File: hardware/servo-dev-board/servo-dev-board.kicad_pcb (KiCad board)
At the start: 2 copper layers, 50 x 30 mm, 39 parts, among them J1 Conn_01x04, J2 Conn_01x05, J3 Conn_01x04, J4 Conn_02x05_Odd_Even, SW1 SW_Push, SW2 SW_Push, U1 DRV8231ADSGR, U2 SSP7615-33DFR, U3 STM32F301K8Ux, Y1 16MHz 9pF

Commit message: design pcb
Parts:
- removed D1: SS34, Diode_SMD:D_SMA
- removed H3, H4, H5, H6: MountingHole, MountingHole:MountingHole_2.2mm_M2_DIN965_Pad
- added MH1: MountingHole_Pad_MP, MountingHole:MountingHole_2.2mm_M2_Pad_Via, F.Cu at (118.0, 93.0)
- added MH2: MountingHole_Pad_MP, MountingHole:MountingHole_2.2mm_M2_Pad_Via, F.Cu at (118.0, 109.0)
- added MH3: MountingHole_Pad_MP, MountingHole:MountingHole_2.2mm_M2_Pad_Via, F.Cu at (162.0, 109.0)
- added MH4: MountingHole_Pad_MP, MountingHole:MountingHole_2.2mm_M2_Pad_Via, F.Cu at (162.0, 93.0)
- J2: value Conn_01x05 -> Conn_01x05_MountingPin; footprint Connector_JST:JST_SH_SM05B-SRSS-TB_1x05-1MP_P1.00mm_Horizontal -> Connector_JST:JST_ZH_B5B-ZR-SM4-TF_1x05-1MP_P1.50mm_Vertical
- J3: value Conn_01x04 -> Conn_01x04_MountingPin
- J4: renamed from J1; value Conn_01x04 -> Conn_01x04_MountingPin
- moved R7 93.7 mm to (127.3, 97.8), turned to -90 degrees
- moved R6 93.0 mm to (122.3, 111.3), turned to 90 degrees
- moved C10 89.5 mm to (142.9, 101.8), turned to 90 degrees
- moved L1 85.1 mm to (141.9, 101.8), turned to -90 degrees
- moved C5 84.7 mm to (123.4, 101.1), turned to 90 degrees
- moved C9 83.8 mm to (143.9, 101.8), turned to 90 degrees
- moved R5 82.2 mm to (128.2, 106.7)
- moved C4 81.7 mm to (123.0, 97.4)
- moved C8 79.1 mm to (146.3, 95.7), turned to 180 degrees
- moved C2 76.2 mm to (122.3, 90.7), turned to 90 degrees
- moved C3 74.6 mm to (121.3, 111.3), turned to 90 degrees
- moved C6 70.0 mm to (145.7, 97.0), turned to 180 degrees
- moved C7 67.7 mm to (150.2, 104.4)
- moved C1 65.3 mm to (124.4, 101.1), turned to 90 degrees
- moved R4 49.5 mm to (155.9, 106.4), turned to 180 degrees
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- renumbered USB1 to J1, J4 to J5
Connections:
- net /OSC_IN renamed /OSC-
- net /OSC_OUT renamed /OSC+
- J1 pad 1: /VBUS -> +5V
- J2 pad 1: /M1 -> /POT
- J2 pad 2: /M2 -> /VREF
- J2 pad 3: /VREF -> GND
- J2 pad 4: GND -> /M1
- J2 pad 5: /POT -> /M2
- J2 pad MP: (no net) -> GND
- J3 pad MP: (no net) -> GND
- J4 pad 1: /UART1_TX -> /UART1_RX
- J4 pad 3: /UART1_RX -> /UART1_TX
- J4 pad MP: (no net) -> GND
- R1 pad 1: /UART1_TX -> /UART1_RX
- R4 pad 1: /UART1_RX -> /UART1_TX
- U1 pad 4: /VREF -> +3V3
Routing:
- net /BOOT0: track 0.00 -> 52.9 mm, vias 0 -> 2
- net GND: track 0.00 -> 44.9 mm, vias 0 -> 37
- net /PWM2: track 0.00 -> 44.4 mm, vias 0 -> 2
- net /PWM1: track 0.00 -> 40.9 mm, vias 0 -> 2
- net +3V3: track 0.00 -> 31.9 mm, vias 0 -> 13
- net /ISNS: track 0.00 -> 30.5 mm, vias 0 -> 2
- net /NRST: track 0.00 -> 29.1 mm
- net /VREF: track 0.00 -> 22.4 mm, vias 0 -> 2
- net /I2C1_SDA: track 0.00 -> 19.2 mm
- net /PA2: track 0.00 -> 18.1 mm
- net /JTCK_SWCLK: track 0.00 -> 17.6 mm
- net /JTDO_SWO: track 0.00 -> 17.5 mm
- net /NJTRST: track 0.00 -> 16.4 mm
- net /PA3: track 0.00 -> 16.3 mm
- net /JTMS_SWDIO: track 0.00 -> 16.0 mm
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- added copper zone on In2.Cu, net +3V3
- added copper zone on F.Cu, net +5V
- added copper zone on In1.Cu, net GND
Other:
- board size 50 x 30 mm -> 51.5 x 23.5 mm
- copper layers 2 -> 4
- board text added: "."
- board text added: "3V3"
- board text added: "5V"
- board text added: "A12"
- board text added: "A2"
- board text added: "A3"
- board text added: "A4"
- board text added: "A5"
- board text added: "A6"
- board text added: "A7"
- board text added: "B0"
- board text added: "B5"
- board text added: "BOOT0"
- board text added: "G"
- board text added: "I2C"
- board text added: "JTAG/SWD"
- board text added: "MOTOR"
- board text added: "PWR"
- board text added: "RESET"
- board text added: "UART"
- board text added: "USB"
- board text added: "VREF"

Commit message: update servo-dev-board
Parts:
- added C11: 22uF, Capacitor_SMD:C_0603_1608Metric, F.Cu at (123.8, 98.8)
- J5: footprint Connector_PinSocket_1.27mm:PinSocket_2x05_P1.27mm_Vertical_SMD -> lib:IDC-TH_10P-P1.27-X1270WV-2X05A-6TV01
- R1, R2, R3, R4, R6: value 10K -> 4K7
- U1: footprint Package_SON:WSON-8-1EP_2x2mm_P0.5mm_EP0.9x1.6mm_ThermalVias -> Package_SON:WSON-8-1EP_2x2mm_P0.5mm_EP0.9x1.6mm
- moved C4 7.23 mm to (123.2, 104.6), turned to 180 degrees
- moved R7 5.27 mm to (131.1, 94.1), turned to 0 degrees
- moved U2 4.00 mm to (123.1, 103.1), turned to 90 degrees
- moved C5 2.30 mm to (124.4, 103.2)
- moved C1 1.78 mm to (125.0, 99.4)
- moved U1 1.66 mm to (125.8, 96.8)
- moved J3 1.55 mm to (154.9, 90.8)
- moved R2 1.55 mm to (157.8, 94.0)
- moved R3 1.55 mm to (155.9, 94.0)
- moved C2 1.52 mm to (122.3, 89.2)
- moved SW1 1.52 mm to (125.7, 90.1)
- moved J4 1.50 mm to (154.9, 111.1)
- moved MH1 1.50 mm to (118.0, 91.5)
- moved MH2 1.50 mm to (118.0, 110.5)
- moved MH3 1.50 mm to (162.0, 110.5)
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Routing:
- net GND: track 44.9 -> 16.4 mm, vias 37 -> 59
- net +3V3: track 31.9 -> 7.02 mm, vias 13 -> 16
- net +5V: track 15.8 -> 27.9 mm
- net /BOOT0: track 52.9 -> 40.8 mm
- net /M1: track 11.0 -> 0.00 mm
- net /M2: track 9.67 -> 0.00 mm
- net /PWM2: track 44.4 -> 36.7 mm
- net /NRST: track 29.1 -> 36.7 mm, vias 0 -> 2
- net /JTCK_SWCLK: track 17.6 -> 13.1 mm
- net /PWM1: track 40.9 -> 37.0 mm
- net /JTMS_SWDIO: track 16.0 -> 13.4 mm
- net /JTDO_SWO: track 17.5 -> 14.9 mm
- net /PA12: track 12.2 -> 14.0 mm
- net /NJTRST: track 16.4 -> 14.7 mm
- net /UART1_TX: track 11.1 -> 12.6 mm
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- added copper zone on F.Cu, net /M1
- added copper zone on F.Cu, net /M2
- added copper zone on B.Cu, net GND
- added copper zone on F.Cu, net GND
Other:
- board size 51.5 x 23.5 mm -> 51.5 x 26.5 mm
- board text added: "JLCJLCJLCJLC"
- board text added: "SERVO"
- board text added: "VRF"
- board text removed: "."
- board text removed: "MOTOR"
- board text removed: "VREF"

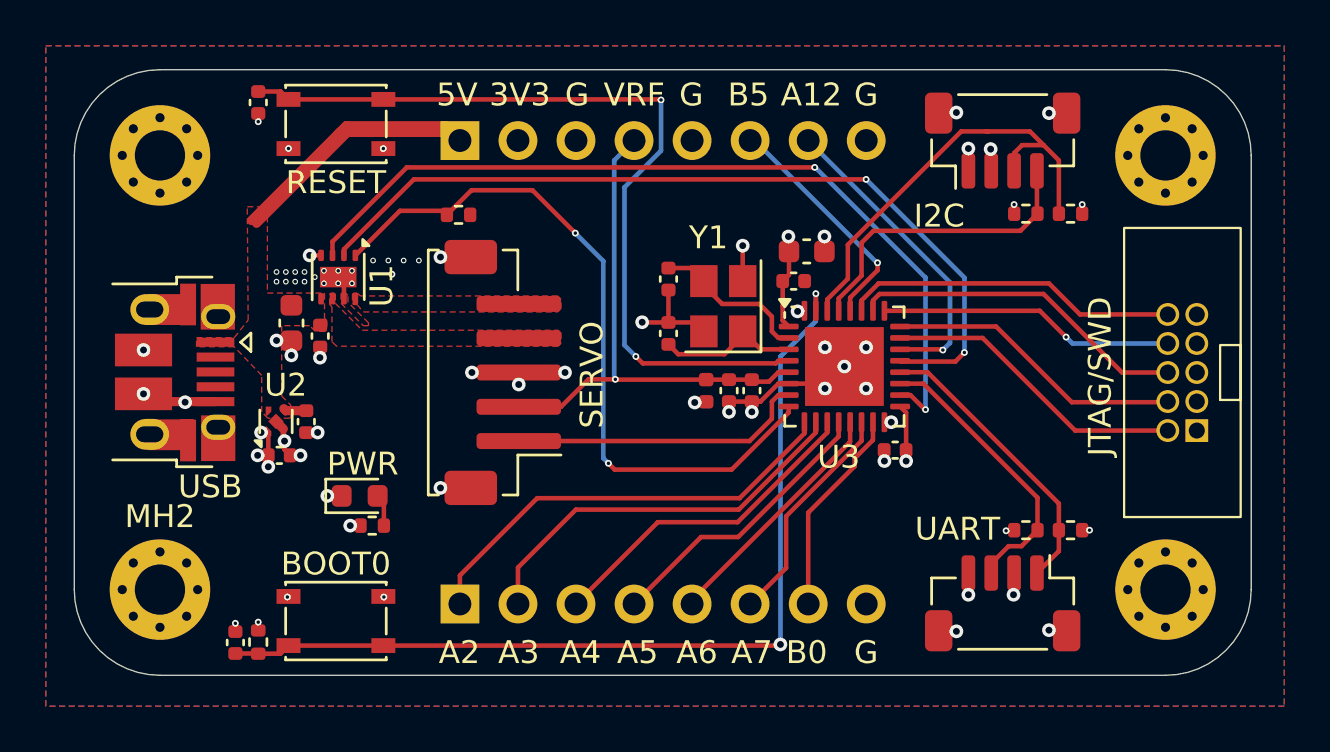
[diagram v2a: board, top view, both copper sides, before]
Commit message: rework vias according updated constraints from jlc pcb
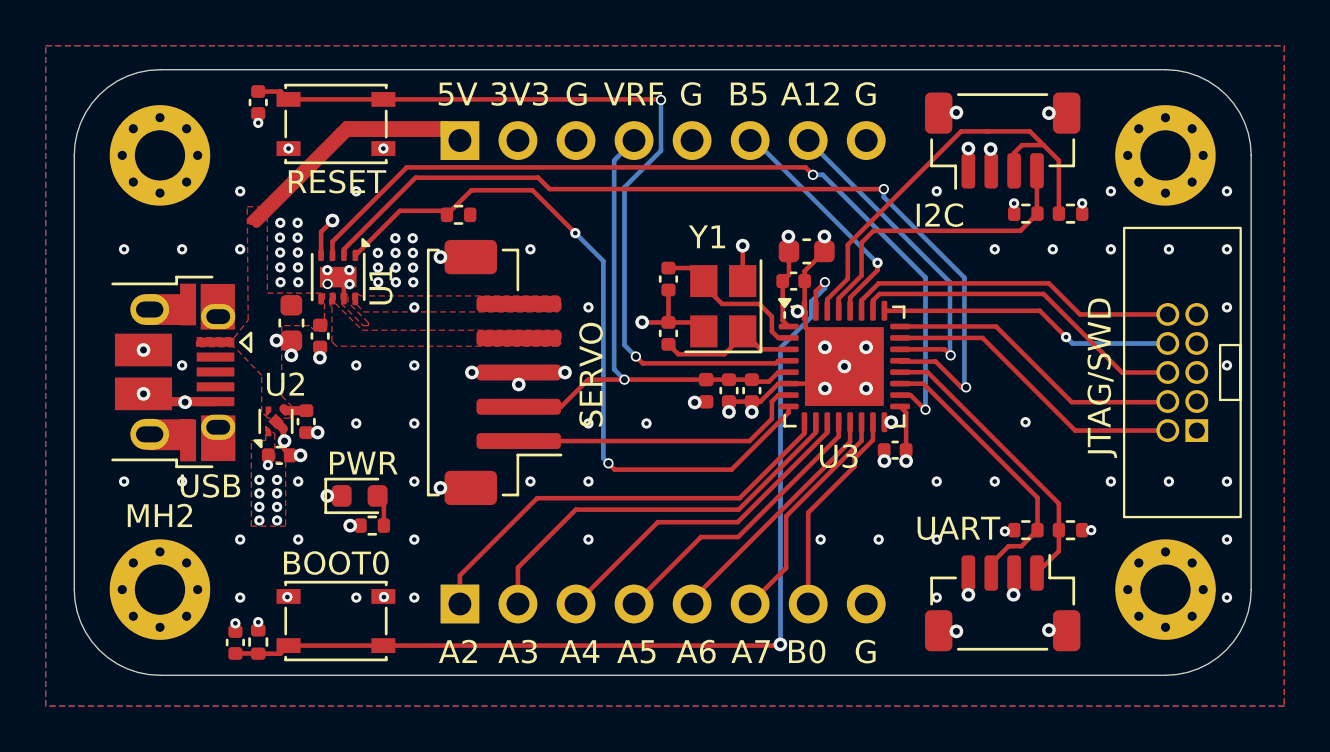
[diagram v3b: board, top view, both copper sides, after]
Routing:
- net GND: track 16.4 -> 22.5 mm, vias 59 -> 114
- net /PWM2: track 36.7 -> 38.9 mm
- net /BOOT0: track 40.8 -> 42.1 mm
- net /PA12: track 14.0 -> 14.6 mm
- net +3V3: track 7.02 -> 7.30 mm, vias 16 -> 22
- added copper zone on F.Cu, net +3V3
